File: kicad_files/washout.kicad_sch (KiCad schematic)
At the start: 0 parts

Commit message: UI, washout detection, motor schematics finished
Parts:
- added C10: 10uF, symbol Device:C
- added C11: 1uF, symbol Device:C
- added C7, C8, C9: 10nF, symbol Device:C
- added D3: 1N914, Diode_THT:D_DO-35_SOD27_P7.62mm_Horizontal, symbol Diode:1N914
- added R13, R16, R17, R18, R19: 100k, symbol Device:R_US
- added R14: 200k, symbol Device:R_US
- added R15: 470k, symbol Device:R_US
- added R20: 20k, symbol Device:R_US
- added U4: LM311, symbol Comparator:LM311
- added U5, U6: LMC555CMMX_NOPB, LMC555CMMX_NOPB:SOP65P490X110-8N, symbol LMC555CMMX_NOPB:LMC555CMMX_NOPB
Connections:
- new net: U4.7, U6.2 (~{TRIGGER})
- new net: R19.1, U6.3 (OUTPUT)
- new net: C10.1, U6.5 (CONTROL_VOLTAGE)
- new net: C9.1, R16.2, U6.6 (THRESHOLD), U6.7 (DISCHARGE)
- new net: R17.2, R18.1, U5.7 (DISCHARGE)
- new net: C8.1, R18.2, U5.2 (~{TRIGGER}), U5.6 (THRESHOLD)
- new net: R13.2, R20.1, U4.2 (+)
- new net: C7.1, U5.5 (CONTROL_VOLTAGE)
- new net: C11.1, D3.1 (K), R15.1, U4.3 (-)
- new net 5V: R13.1, R16.1, R17.1, U4.8 (V+), U5.4 (~{RESET}), U5.8 (V+), U6.4 (~{RESET}), U6.8 (V+)
- new net MCU_in: R14.1, R19.2
- new net Screw1: U5.3 (OUTPUT)
- new net Screw2: D3.2 (A)
- new net gnd: C10.2, C11.2, C7.2, C8.2, C9.2, R14.2, R15.2, R20.2, U4.4 (V-), U5.1 (GND), U6.1 (GND)

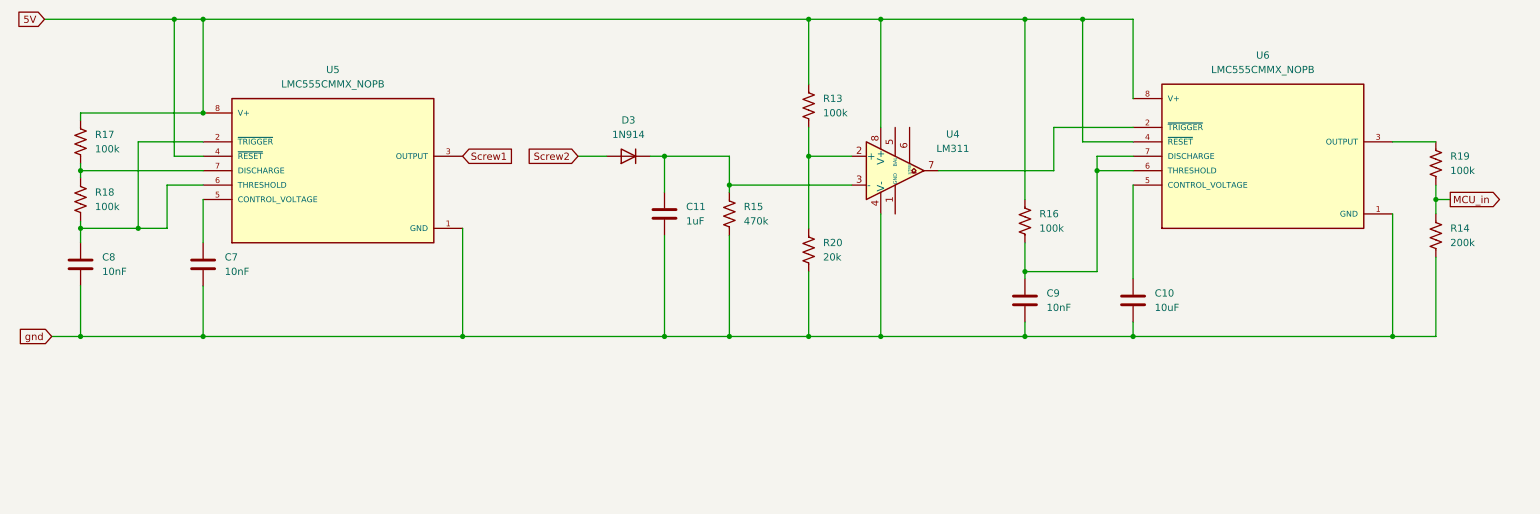
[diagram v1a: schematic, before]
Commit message: Hierarchical labels finished. Flyback diode issue fixed. I2C pins added
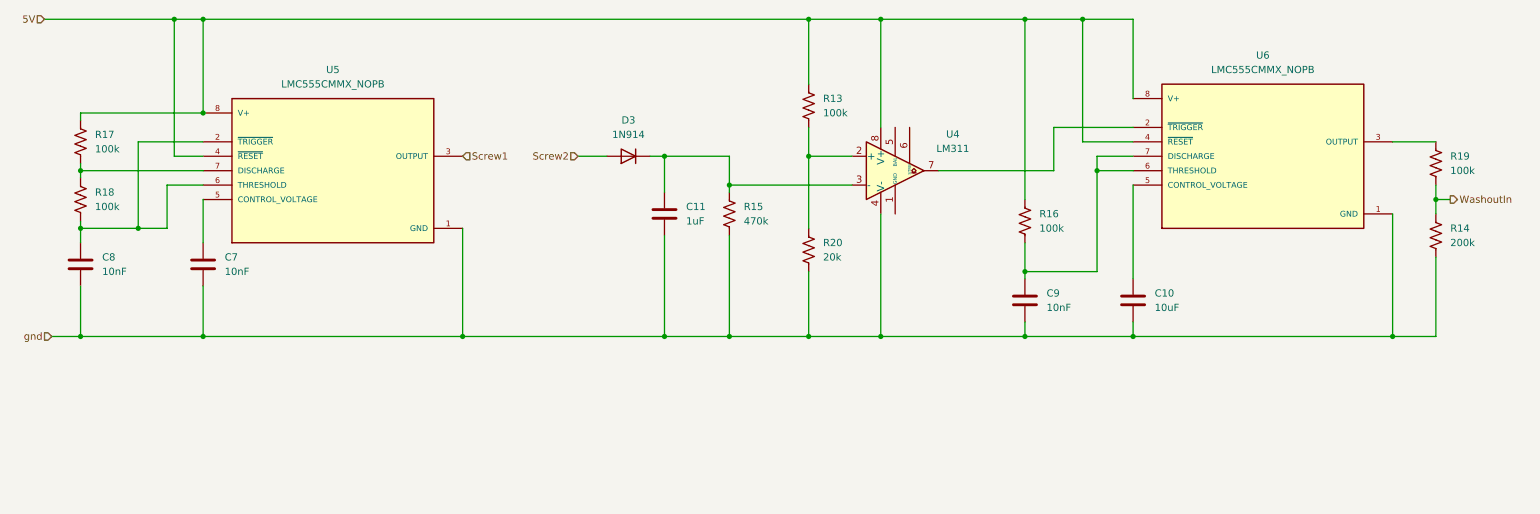
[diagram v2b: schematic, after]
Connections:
- net MCU_in renamed WashoutIn
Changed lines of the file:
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@@
 		)
 	)
-	(global_label "gnd"
+	(hierarchical_label "5V"
 		(shape input)
-		(at 26.67 137.16 180)
-		(fields_autoplaced yes)
+		(at 25.4 81.28 180)
 		(effects
 			(font
@@
 			(justify right)
 		)
-		(property "Intersheetrefs" "${INTERSHEET_REFS}"
-			(at 20.2378 137.16 0)
-			(effects
-				(font
-					(size 1.27 1.27)
-				)
-				(justify right)
-				(hide yes)
+	)
+	(hierarchical_label "gnd"
+		(shape input)
+		(at 26.67 137.16 180)
+		(effects
+			(font
+				(size 1.27 1.27)
 			)
+			(justify right)
 		)
 	)
-	(global_label "MCU_in"
+	(hierarchical_label "Screw2"
+		(shape input)
+		(at 119.38 105.41 180)
+		(effects
+			(font
+				(size 1.27 1.27)
+			)
+			(justify right)
+		)
+	)
+	(hierarchical_label "WashoutIn"
 		(shape output)
 		(at 273.05 113.03 0)
-		(fields_autoplaced yes)
 		(effects
 			(font
@@
 			(justify left)
 		)
-		(property "Intersheetrefs" "${INTERSHEET_REFS}"
-			(at 282.8085 113.03 0)
-			(effects
-				(font
-					(size 1.27 1.27)
-				)
-				(justify left)
-				(hide yes)
-			)
-		)
 	)
-	(global_label "Screw1"
+	(hierarchical_label "Screw1"
 		(shape input)
 		(at 99.06 105.41 0)
-		(fields_autoplaced yes)
 		(effects
 			(font
@@
 			(justify left)
 		)
-		(property "Intersheetrefs" "${INTERSHEET_REFS}"
-			(at 108.7581 105.41 0)
-			(effects
-				(font
-					(size 1.27 1.27)
-				)
-				(justify left)
-				(hide yes)
-			)
-		)
 	)
-	(global_label "5V"
-		(shape input)
-		(at 25.4 81.28 180)
-		(fields_autoplaced yes)
-		(effects
-			(font
-				(size 1.27 1.27)
-			)
-			(justify right)
-		)
-		(property "Intersheetrefs" "${INTERSHEET_REFS}"
-			(at 20.1167 81.28 0)
-			(effects
-				(font
-					(size 1.27 1.27)
-				)
-				(justify right)
-				(hide yes)
-			)
-		)
-	)
-	(global_label "Screw2"
-		(shape input)
-		(at 119.38 105.41 180)
-		(fields_autoplaced yes)
-		(effects
-			(font
-				(size 1.27 1.27)
-			)
-			(justify right)
-		)
-		(property "Intersheetrefs" "${INTERSHEET_REFS}"
-			(at 109.6819 105.41 0)
-			(effects
-				(font
-					(size 1.27 1.27)
-				)
-				(justify right)
-				(hide yes)
-			)
-		)
-	)

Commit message: Partial footprint assignment
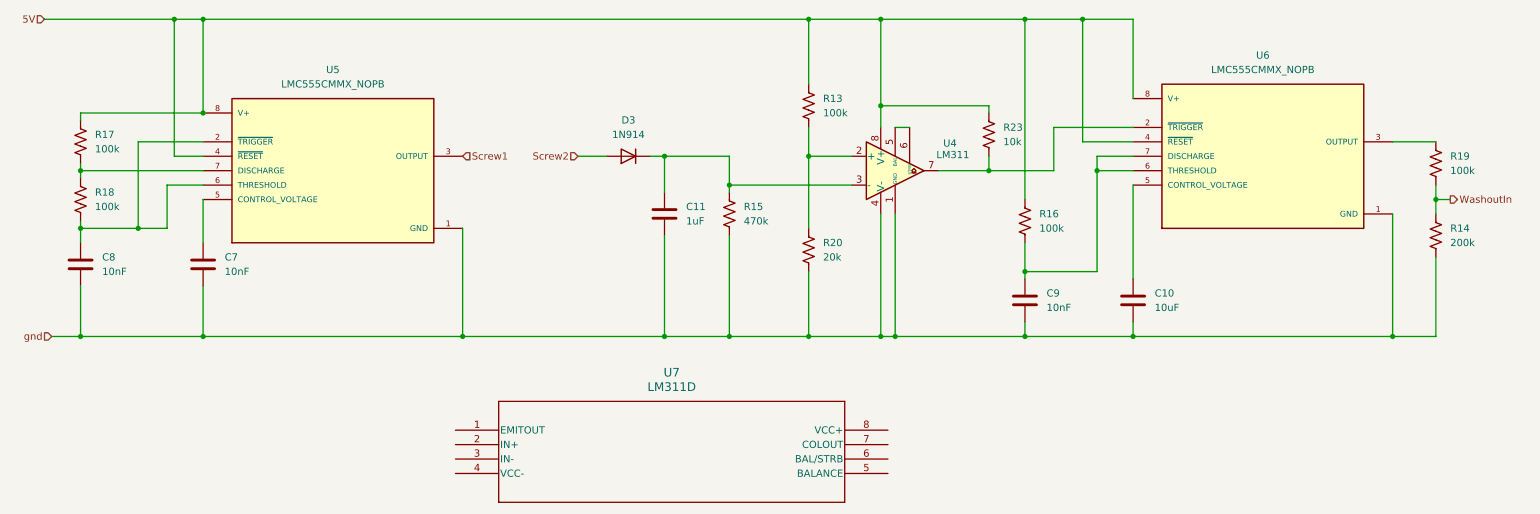
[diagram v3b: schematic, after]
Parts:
- added R23: 10k, symbol Device:R_US
- added U7: LM311D, LM311:D8, symbol LM311:LM311D
- U4: footprint (none) -> LM311:D8
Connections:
- net 5V: now also R23.1
- net gnd: now also U4.1 (GND)
- net at U4.7, U6.2 (~{TRIGGER}): now also R23.2
- net at U4.5 (BAL): now also U4.6 (STRB)

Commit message: ERC errors cleaned. Hierarchical wiring finished. PWM converter change. Motor driver change.
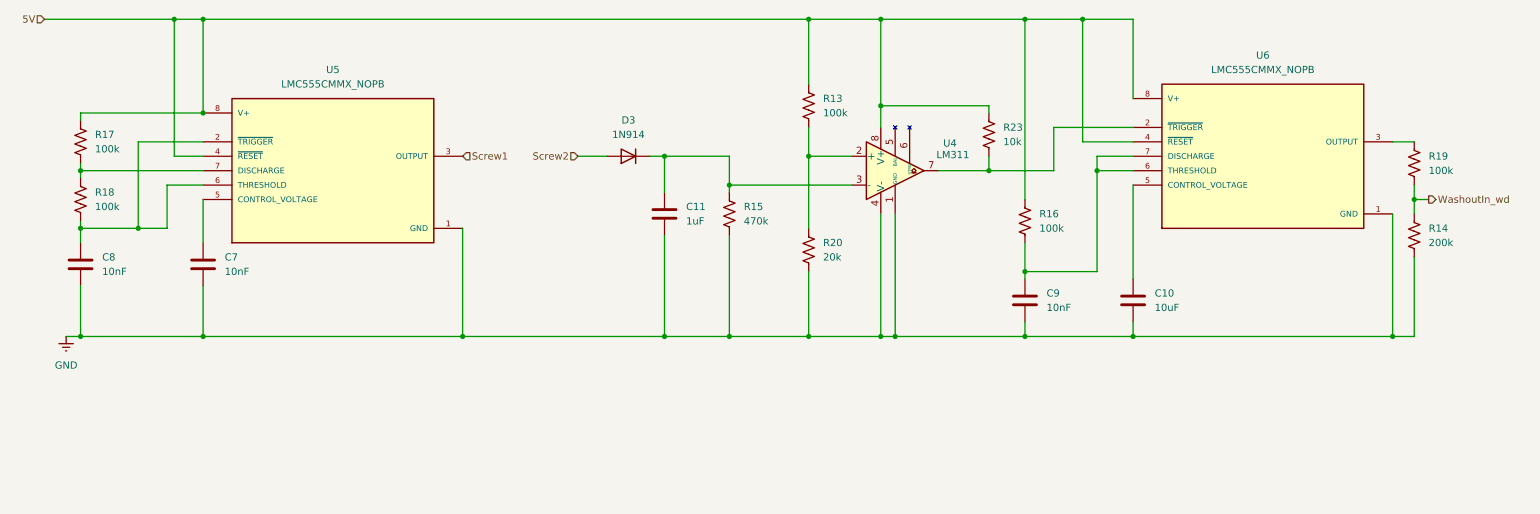
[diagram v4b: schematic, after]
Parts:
- removed U7: LM311D, LM311:D8, symbol LM311:LM311D
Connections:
- net at U4.5 (BAL): no longer U4.6 (STRB)
- net WashoutIn renamed WashoutIn_wd
- net gnd renamed GND
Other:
- moved on the sheet: R14, R19
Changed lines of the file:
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@@
-	)
-	(junction
-		(at 270.51 113.03)
-		(diameter 0)
-		(color 0 0 0 0)
 	)
 	(junction
@@
 		(color 0 0 0 0)
 	)
+	(junction
+		(at 266.7 113.03)
+		(diameter 0)
+		(color 0 0 0 0)
+	)
 	(wire
 		(pts
@@
 	(wire
 		(pts
-			(xy 270.51 110.49) (xy 270.51 113.03)
-		)
-		(stroke
-			(width 0)
-			(type default)
-		)
-	)
-	(wire
-		(pts
 			(xy 217.17 102.87) (xy 208.28 102.87)
 		)
@@
 	(wire
 		(pts
+			(xy 262.89 137.16) (xy 266.7 137.16)
+		)
+		(stroke
+			(width 0)
+			(type default)
+		)
+	)
+	(wire
+		(pts
+			(xy 29.21 137.16) (xy 31.75 137.16)
+		)
+		(stroke
+			(width 0)
+			(type default)
+		)
+	)
+	(wire
+		(pts
 			(xy 191.77 107.95) (xy 203.2 107.95)
 		)
@@
 	(wire
 		(pts
-			(xy 175.26 100.33) (xy 177.8 100.33)
-		)
-		(stroke
-			(width 0)
-			(type default)
-		)
-	)
-	(wire
-		(pts
 			(xy 48.26 81.28) (xy 53.34 81.28)
 		)
@@
 	(wire
 		(pts
-			(xy 273.05 113.03) (xy 270.51 113.03)
+			(xy 266.7 113.03) (xy 266.7 115.57)
 		)
 		(stroke
@@
 	(wire
 		(pts
-			(xy 262.89 137.16) (xy 270.51 137.16)
-		)
-		(stroke
-			(width 0)
-			(type default)
-		)
-	)
-	(wire
-		(pts
 			(xy 53.34 105.41) (xy 48.26 105.41)
 		)
@@
 	(wire
 		(pts
-			(xy 26.67 137.16) (xy 31.75 137.16)
-		)
-		(stroke
-			(width 0)
-			(type default)
-		)
-	)
-	(wire
-		(pts
 			(xy 134.62 137.16) (xy 146.05 137.16)
 		)
@@
 	(wire
 		(pts
+			(xy 269.24 113.03) (xy 266.7 113.03)
+		)
+		(stroke
+			(width 0)
+			(type default)
+		)
+	)
+	(wire
+		(pts
 			(xy 210.82 125.73) (xy 198.12 125.73)
 		)
@@
 	(wire
 		(pts
-			(xy 270.51 123.19) (xy 270.51 137.16)
+			(xy 266.7 123.19) (xy 266.7 137.16)
 		)
 		(stroke
@@
 	(wire
 		(pts
-			(xy 270.51 113.03) (xy 270.51 115.57)
+			(xy 266.7 110.49) (xy 266.7 113.03)
 		)
 		(stroke
@@
 	(wire
 		(pts
-			(xy 262.89 102.87) (xy 270.51 102.87)
-		)
-		(stroke
-			(width 0)
-			(type default)
-		)
-	)
-	(wire
-		(pts
 			(xy 191.77 96.52) (xy 172.72 96.52)
 		)
@@
 		(pts
 			(xy 119.38 105.41) (xy 124.46 105.41)
+		)
+		(stroke
+			(width 0)
+			(type default)
+		)
+	)
+	(wire
+		(pts
+			(xy 262.89 102.87) (xy 266.7 102.87)
 		)
 		(stroke
@@
 		)
 	)
-	(hierarchical_label "gnd"
-		(shape input)
-		(at 26.67 137.16 180)
-		(effects
-			(font
-				(size 1.27 1.27)
-			)
-			(justify right)
-		)
-	)
 	(hierarchical_label "Screw2"
 		(shape input)
@@
 		)
 	)
-	(hierarchical_label "WashoutIn"
+	(hierarchical_label "WashoutIn_wd"
 		(shape output)
-		(at 273.05 113.03 0)
+		(at 269.24 113.03 0)
 		(effects
 			(font
@@
 	)
 	(symbol
-		(lib_id "LM311:LM311D")
-		(at 97.79 153.67 0)
-		(unit 1)
-		(exclude_from_sim no)
-		(in_bom yes)
-		(on_board yes)
-		(dnp no)
-		(fields_autoplaced yes)
-		(property "Reference" "U7"
-			(at 135.89 143.51 0)
-			(effects
-				(font
-					(size 1.524 1.524)
-				)
-			)
-		)
-		(property "Value" "LM311D"
-			(at 135.89 146.05 0)
-			(effects
-				(font
-					(size 1.524 1.524)
-				)
-			)
-		)
-		(property "Footprint" "LM311:D8"
-			(at 97.79 153.67 0)
-			(effects
-				(font
-					(size 1.27 1.27)
-					(italic yes)
-				)
-				(hide yes)
-			)
-		)
-		(property "Datasheet" "https://www.ti.com/lit/gpn/lm311"
-			(at 97.79 153.67 0)
-			(effects
-				(font
-					(size 1.27 1.27)
-					(italic yes)
-				)
-				(hide yes)
-			)
-		)
-		(property "Description" ""
-			(at 97.79 153.67 0)
-			(effects
-				(font
-					(size 1.27 1.27)
-				)
-				(hide yes)
-			)
-		)
-		(pin "1"
-		)
-		(pin "6"
-		)
-		(pin "4"
-		)
-		(pin "8"
-		)
-		(pin "2"
-		)
-		(pin "3"
-		)
-		(pin "7"
-		)
-		(pin "5"
-		)
-		(instances
-			(project ""
-				(path "/67de3bec-6c8a-4e66-9cf7-9a8a92865209/af888bc5-e77d-4cd8-a96c-c672ae10409a"
-					(reference "U7")
-					(unit 1)
-				)
-			)
-		)
-	)
-	(symbol
 		(lib_id "Device:R_US")
 		(at 31.75 113.03 0)
@@
 	)
 	(symbol
+		(lib_id "power:GNDREF")
+		(at 29.21 137.16 0)
+		(unit 1)
+		(exclude_from_sim no)
+		(in_bom yes)
+		(on_board yes)
+		(dnp no)
+		(fields_autoplaced yes)
+		(property "Reference" "#PWR07"
+			(at 29.21 143.51 0)
+			(effects
+				(font
+					(size 1.27 1.27)
+				)
+				(hide yes)
+			)
+		)
+		(property "Value" "GND"
+			(at 29.21 142.24 0)
+			(effects
+				(font
+					(size 1.27 1.27)
+				)
+			)
+		)
+		(property "Footprint" ""
+			(at 29.21 137.16 0)
+			(effects
+				(font
+					(size 1.27 1.27)
+				)
+				(hide yes)
+			)
+		)
+		(property "Datasheet" ""
+			(at 29.21 137.16 0)
+			(effects
+				(font
+					(size 1.27 1.27)
+				)
+				(hide yes)
+			)
+		)
+		(property "Description" "Power symbol creates a global label with name \"GNDREF\" , reference supply ground"
+			(at 29.21 137.16 0)
+			(effects
+				(font
+					(size 1.27 1.27)
+				)
+				(hide yes)
+			)
+		)
+		(pin "1"
+		)
+		(instances
+			(project "kicad_files"
+				(path "/67de3bec-6c8a-4e66-9cf7-9a8a92865209/af888bc5-e77d-4cd8-a96c-c672ae10409a"
+					(reference "#PWR07")
+					(unit 1)
+				)
+			)
+		)
+	)
+	(symbol
 		(lib_id "Device:C")
 		(at 53.34 124.46 0)
@@
 	(symbol
 		(lib_id "Device:R_US")
-		(at 270.51 106.68 0)
+		(at 266.7 106.68 0)
 		(unit 1)
 		(exclude_from_sim no)
@@
 		(fields_autoplaced yes)
 		(property "Reference" "R19"
-			(at 273.05 105.4099 0)
+			(at 269.24 105.4099 0)
 			(effects
 				(font
@@
 		)
 		(property "Value" "100k"
-			(at 273.05 107.9499 0)
+			(at 269.24 107.9499 0)
 			(effects
 				(font
@@
 		)
 		(property "Footprint" ""
-			(at 271.526 106.934 90)
+			(at 267.716 106.934 90)
 			(effects
 				(font
@@
 		)
 		(property "Datasheet" "~"
-			(at 270.51 106.68 0)
+			(at 266.7 106.68 0)
 			(effects
 				(font
@@
 		)
 		(property "Description" "Resistor, US symbol"
-			(at 270.51 106.68 0)
+			(at 266.7 106.68 0)
 			(effects
 				(font
@@
 	(symbol
 		(lib_id "Device:R_US")
-		(at 270.51 119.38 0)
+		(at 266.7 119.38 0)
 		(unit 1)
 		(exclude_from_sim no)
@@
 		(fields_autoplaced yes)
 		(property "Reference" "R14"
-			(at 273.05 118.1099 0)
+			(at 269.24 118.1099 0)
 			(effects
 				(font
@@
 		)
 		(property "Value" "200k"
-			(at 273.05 120.6499 0)
+			(at 269.24 120.6499 0)
 			(effects
 				(font
@@
 		)
 		(property "Footprint" ""
-			(at 271.526 119.634 90)
+			(at 267.716 119.634 90)
 			(effects
 				(font
@@
 		)
 		(property "Datasheet" "~"
-			(at 270.51 119.38 0)
+			(at 266.7 119.38 0)
 			(effects
 				(font
@@
 		)
 		(property "Description" "Resistor, US symbol"
-			(at 270.51 119.38 0)
-			(effects
-				(font
+			(at 266.7 119.38 0)
+			(effects
+				(font

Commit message: Footprint assignment finished
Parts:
- C10, C11, C7, C8, C9: footprint (none) -> Capacitor_SMD:C_1206_3216Metric_Pad1.33x1.80mm_HandSolder
- R13, R14, R15, R16, R17, R18, R19, R20, R23: footprint (none) -> Resistor_SMD:R_1206_3216Metric_Pad1.30x1.75mm_HandSolder
- U5, U6: footprint LMC555CMMX_NOPB:SOP65P490X110-8N -> LMC555CMX_NOPB:D0008A_M
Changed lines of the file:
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@@
 			)
 		)
-		(property "Footprint" "LMC555CMMX_NOPB:SOP65P490X110-8N"
+		(property "Footprint" "LMC555CMX_NOPB:D0008A_M"
 			(at 240.03 105.41 0)
 			(effects
@@
 			)
 		)
-		(property "Footprint" ""
+		(property "Footprint" "Resistor_SMD:R_1206_3216Metric_Pad1.30x1.75mm_HandSolder"
 			(at 32.766 113.284 90)
 			(effects
@@
 			)
 		)
-		(property "Footprint" ""
+		(property "Footprint" "Resistor_SMD:R_1206_3216Metric_Pad1.30x1.75mm_HandSolder"
 			(at 161.036 96.774 90)
 			(effects
@@
 			)
 		)
-		(property "Footprint" ""
+		(property "Footprint" "Capacitor_SMD:C_1206_3216Metric_Pad1.33x1.80mm_HandSolder"
 			(at 54.3052 128.27 0)
 			(effects
@@
 			)
 		)
-		(property "Footprint" ""
+		(property "Footprint" "Resistor_SMD:R_1206_3216Metric_Pad1.30x1.75mm_HandSolder"
 			(at 161.036 122.174 90)
 			(effects
@@
 			)
 		)
-		(property "Footprint" ""
+		(property "Footprint" "Resistor_SMD:R_1206_3216Metric_Pad1.30x1.75mm_HandSolder"
 			(at 199.136 117.094 90)
 			(effects
@@
 			)
 		)
-		(property "Footprint" ""
+		(property "Footprint" "Capacitor_SMD:C_1206_3216Metric_Pad1.33x1.80mm_HandSolder"
 			(at 199.0852 134.62 0)
 			(effects
@@
 			)
 		)
-		(property "Footprint" ""
+		(property "Footprint" "Resistor_SMD:R_1206_3216Metric_Pad1.30x1.75mm_HandSolder"
 			(at 267.716 106.934 90)
 			(effects
@@
 			)
 		)
-		(property "Footprint" ""
+		(property "Footprint" "Capacitor_SMD:C_1206_3216Metric_Pad1.33x1.80mm_HandSolder"
 			(at 135.5852 119.38 0)
 			(effects
@@
 			)
 		)
-		(property "Footprint" ""
+		(property "Footprint" "Capacitor_SMD:C_1206_3216Metric_Pad1.33x1.80mm_HandSolder"
 			(at 32.7152 128.27 0)
 			(effects
@@
 			)
 		)
-		(property "Footprint" "LMC555CMMX_NOPB:SOP65P490X110-8N"
+		(property "Footprint" "LMC555CMX_NOPB:D0008A_M"
 			(at 76.2 107.95 0)
 			(effects
@@
 			)
 		)
-		(property "Footprint" ""
+		(property "Footprint" "Capacitor_SMD:C_1206_3216Metric_Pad1.33x1.80mm_HandSolder"
 			(at 218.1352 134.62 0)
 			(effects
@@
 			)
 		)
-		(property "Footprint" ""
+		(property "Footprint" "Resistor_SMD:R_1206_3216Metric_Pad1.30x1.75mm_HandSolder"
 			(at 147.066 115.824 90)
 			(effects
@@
 			)
 		)
-		(property "Footprint" ""
+		(property "Footprint" "Resistor_SMD:R_1206_3216Metric_Pad1.30x1.75mm_HandSolder"
 			(at 32.766 103.124 90)
 			(effects
@@
 			)
 		)
-		(property "Footprint" ""
+		(property "Footprint" "Resistor_SMD:R_1206_3216Metric_Pad1.30x1.75mm_HandSolder"
 			(at 192.786 101.854 90)
 			(effects
@@
 			)
 		)
-		(property "Footprint" ""
+		(property "Footprint" "Resistor_SMD:R_1206_3216Metric_Pad1.30x1.75mm_HandSolder"
 			(at 267.716 119.634 90)
 			(effects
